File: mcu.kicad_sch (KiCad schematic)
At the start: 61 parts, among them J1 Micro_SD_Card, J1501 USB_B, J1502 Conn_02x05_Odd_Even, J1504 USB_B, J1505 Conn_01x06, J2 Conn_01x02, J4 Conn_01x06, SW1501 SW_Push, SW1502 SW_Push, U1501 STM32F427ZGTx, U1502 USBLC6-2SC6, U8 REF3333, U9 LPS25HB, Y1501 8MHz

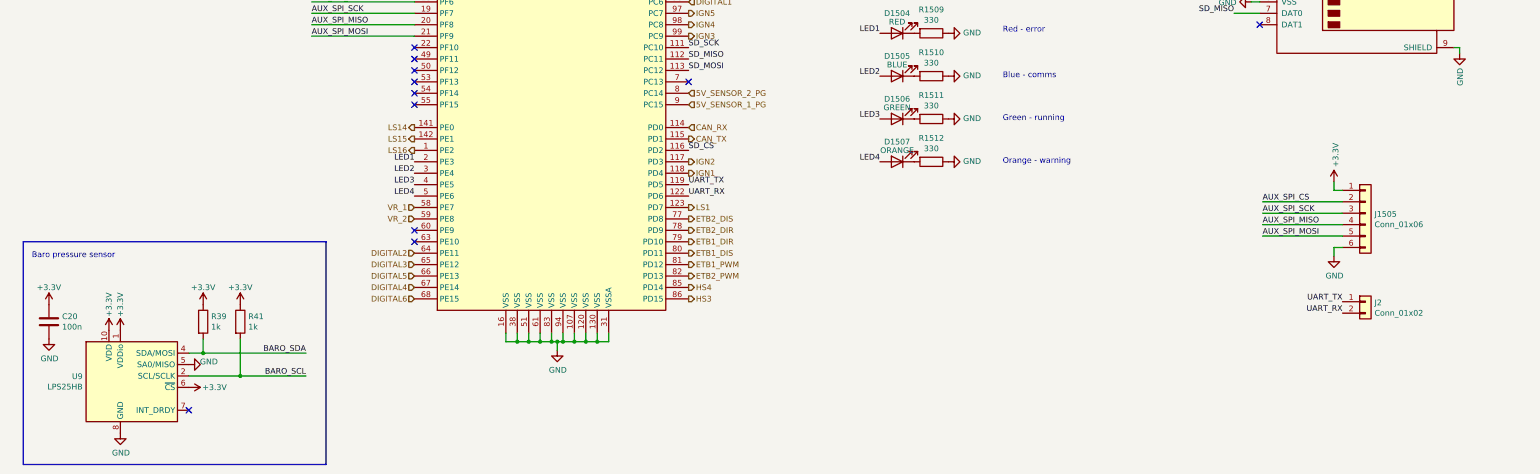
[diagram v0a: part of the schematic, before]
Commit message: File names changed / moved to folders. Updated file names to 1999_Dodge_Dakota Moved files footprints and symbols into a folder
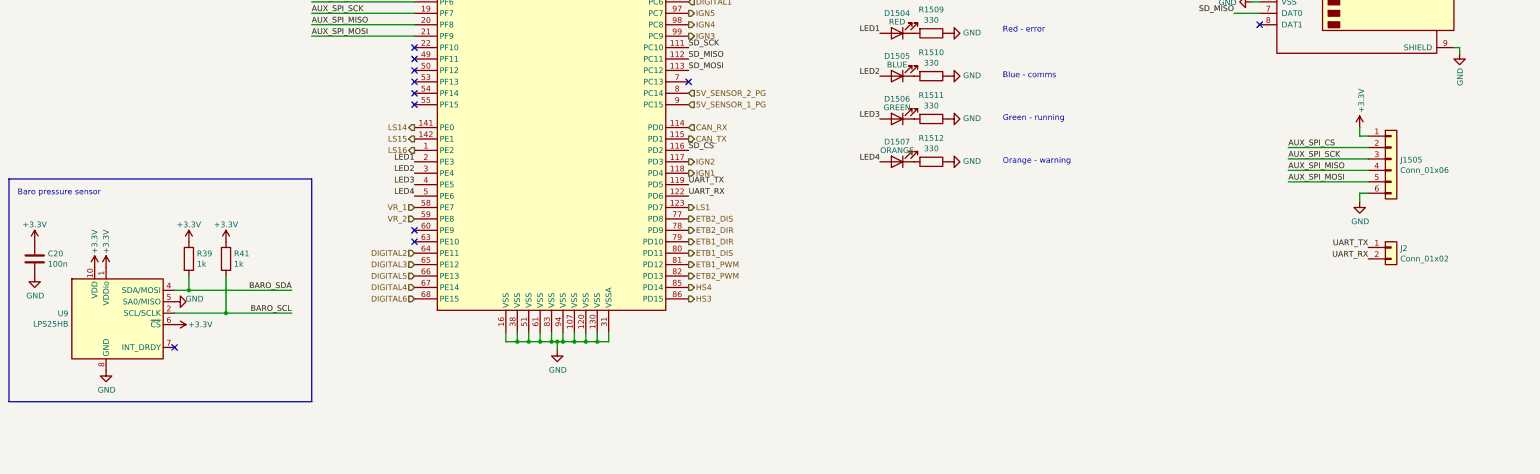
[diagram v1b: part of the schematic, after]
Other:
- title: rusEfi Proteus -> 1999 Dodge Dakota Based on rusEFI/proteus
- moved on the sheet: C20, J1505, J2, R39, R41, U9
